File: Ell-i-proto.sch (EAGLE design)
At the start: 144 parts, among them J1 FTDI-SER-6, J10 PJ-102AX, J2 PWMH, J3 PWR, J4 PWML, J5 ANAL, J6 SPI, J7 COMM, J8 ANAH, J9 RJ45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

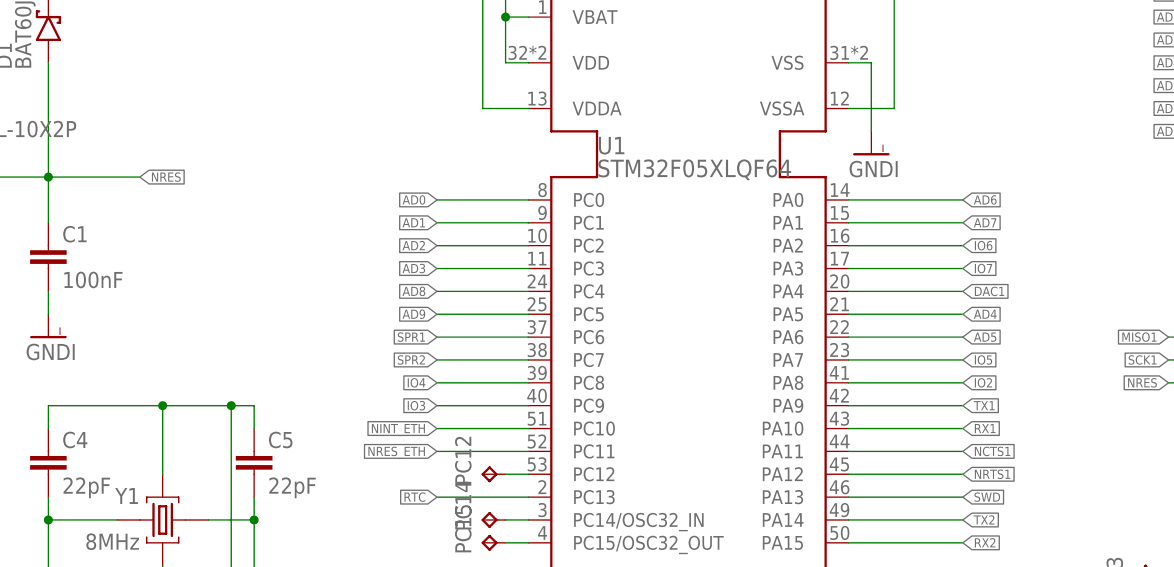
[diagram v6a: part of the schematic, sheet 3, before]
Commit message: drafting the gnd/power planes in inner layers, some routing, ADCs etc
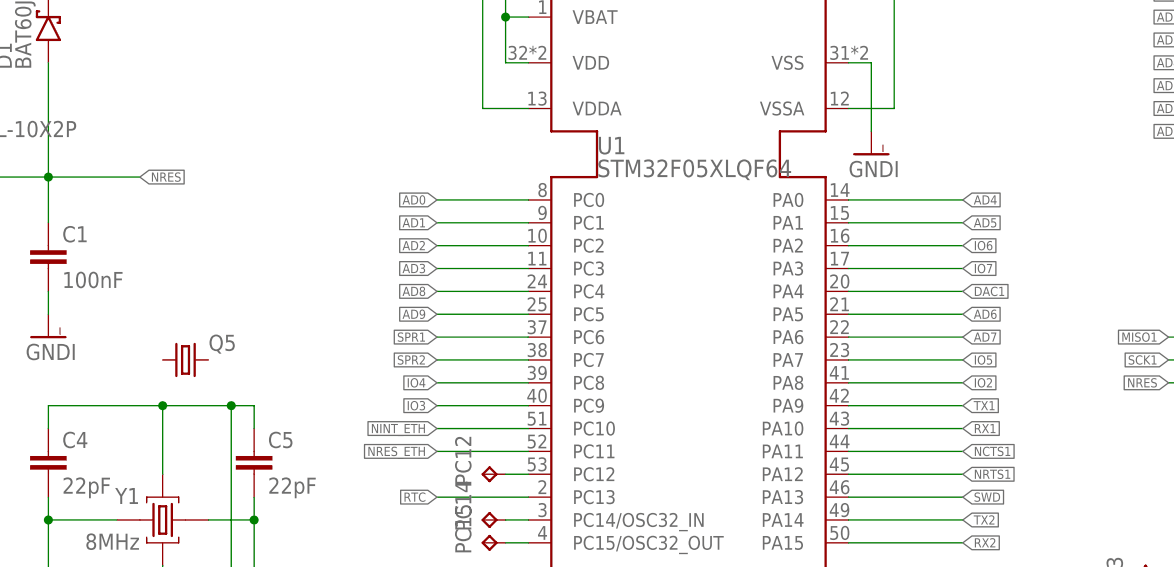
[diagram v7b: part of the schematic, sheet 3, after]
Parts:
- added Q5: (no value), crystal:CRYSTALSM49
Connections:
- net AD4: now also U1.PA0; no longer U1.PA5
- net AD5: now also U1.PA1; no longer U1.PA6
- net AD6: now also U1.PA5; no longer U1.PA0
- net AD7: now also U1.PA6; no longer U1.PA1
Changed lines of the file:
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@@
 </variantdefs>
 <classes>
-<class number="0" name="default" width="0.1524" drill="0.3048">
-<clearance class="0" value="0.1524"/>
+<class number="0" name="default" width="0.1" drill="0.3">
+<clearance class="0" value="0.1"/>
 </class>
-<class number="1" name="power" width="0.508" drill="0.8128">
-<clearance class="1" value="0.2032"/>
+<class number="1" name="power" width="0.5" drill="0.3">
+<clearance class="1" value="0.15"/>
 </class>
 </classes>
@@
 <part name="FID2" library="ell-i" deviceset="MOUNT_FIDUCIAL" device=""/>
 <part name="FID3" library="ell-i" deviceset="MOUNT_FIDUCIAL" device=""/>
+<part name="Q5" library="crystal" deviceset="CRYSTAL" device="SM49"/>
 </parts>
 <sheets>
@@
 <instance part="J1" gate="G$1" x="12.7" y="139.7" rot="MR180"/>
 <instance part="S1" gate="G$1" x="38.1" y="114.3" rot="R270"/>
+<instance part="Q5" gate="G$1" x="66.04" y="93.98"/>
 </instances>
 <busses>
@@
 <net name="AD4" class="0">
 <segment>
-<pinref part="U1" gate="G$1" pin="PA5"/>
-<wire x1="152.4" y1="99.06" x2="139.7" y2="99.06" width="0.1524" layer="91"/>
-<label x="152.4" y="99.06" size="1.016" layer="95" xref="yes"/>
+<wire x1="152.4" y1="111.76" x2="139.7" y2="111.76" width="0.1524" layer="91"/>
+<label x="152.4" y="111.76" size="1.016" layer="95" xref="yes"/>
+<pinref part="U1" gate="G$1" pin="PA0"/>
 </segment>
 <segment>
@@
 <net name="AD5" class="0">
 <segment>
-<pinref part="U1" gate="G$1" pin="PA6"/>
-<wire x1="152.4" y1="96.52" x2="139.7" y2="96.52" width="0.1524" layer="91"/>
-<label x="152.4" y="96.52" size="1.016" layer="95" xref="yes"/>
+<wire x1="152.4" y1="109.22" x2="139.7" y2="109.22" width="0.1524" layer="91"/>
+<label x="152.4" y="109.22" size="1.016" layer="95" xref="yes"/>
+<pinref part="U1" gate="G$1" pin="PA1"/>
 </segment>
 <segment>
@@
 <net name="AD6" class="0">
 <segment>
-<pinref part="U1" gate="G$1" pin="PA0"/>
-<wire x1="152.4" y1="111.76" x2="139.7" y2="111.76" width="0.1524" layer="91"/>
-<label x="152.4" y="111.76" size="1.016" layer="95" xref="yes"/>
+<wire x1="152.4" y1="99.06" x2="139.7" y2="99.06" width="0.1524" layer="91"/>
+<label x="152.4" y="99.06" size="1.016" layer="95" xref="yes"/>
+<pinref part="U1" gate="G$1" pin="PA5"/>
 </segment>
 <segment>
@@
 <net name="AD7" class="0">
 <segment>
-<pinref part="U1" gate="G$1" pin="PA1"/>
-<wire x1="152.4" y1="109.22" x2="139.7" y2="109.22" width="0.1524" layer="91"/>
-<label x="152.4" y="109.22" size="1.016" layer="95" xref="yes"/>
-</segment>
-<segment>
+<wire x1="152.4" y1="96.52" x2="139.7" y2="96.52" width="0.1524" layer="91"/>
+<label x="152.4" y="96.52" size="1.016" layer="95" xref="yes"/>
+<pinref part="U1" gate="G$1" pin="PA6"/>
+</segment>
+<segment>

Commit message: all lines somehow routed and seem to fit to the board, some parts updated, etc
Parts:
- removed Q5: (no value), crystal:CRYSTALSM49
- added C45, C46, C47, C48: 22u, ell-i:C0805
- C13: value 10uF -> 22uF; device ell-i:C0603 -> ell-i:C0805
- C34: value 100uF -> 22u; device rcl:C-EUC1206 -> ell-i:C0805
- H1, H2, H3, H4, H5, H6: value MOUNT-HOLE3.2 -> MOUNT_HOLE; device holes:MOUNT-HOLE3.2 -> ell-i:MOUNT_HOLE
- J1: value FTDI-SER-6 -> TSM-106-01-L-SH; device ell-i:FTDI-SER-6 -> ell-i:TSM-106-01-L-SH
- J10: value PJ-102AX -> KLDX-SMT2-0202; device ell-i:PJ-102AX -> ell-i:KLDX-SMT2-0202
- J9: device ell-i:43860-0001 -> ell-i:85502-5008
- S1: value B3SL-10X2P -> EVQQ2/P0; device ell-i:B3SL-10X2P -> ell-i:EVQQ2/P0
- Y1: value 8MHz -> (none); device ell-i:XTAL3225 -> crystal:CRYSTALSM49
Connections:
- net +5V: now also C45.1, C46.1, C47.1, C48.1
- net GNDI: now also C45.2, C46.2, C47.2, C48.2, J1.6; no longer J1.GND, Y1.GND@1, Y1.GND@2
- net N$6: now also J1.5; no longer J1.-CTS
- net N205481: now also Y1.1; no longer Y1.C2
- net NDSR2: now also J1.1; no longer J1.-RTS
- net PE: now also J9.S1, J9.S2
- net PF0: now also Y1.2; no longer Y1.C1
- net RX2: now also J1.3; no longer J1.TXD
- net TX2: now also J1.2; no longer J1.RXD
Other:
- note added: "Fiducials for automated assembly"
- moved on the sheet: H3, H4, H5, H6, J10
